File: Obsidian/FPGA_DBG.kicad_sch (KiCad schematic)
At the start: 24 parts, among them Q3 BSS138LT1G, SW1 SW_DIP_x01, U1 XC7A35T-CSG325, U27 S25FL128SAGMFI001, U9 REF3012

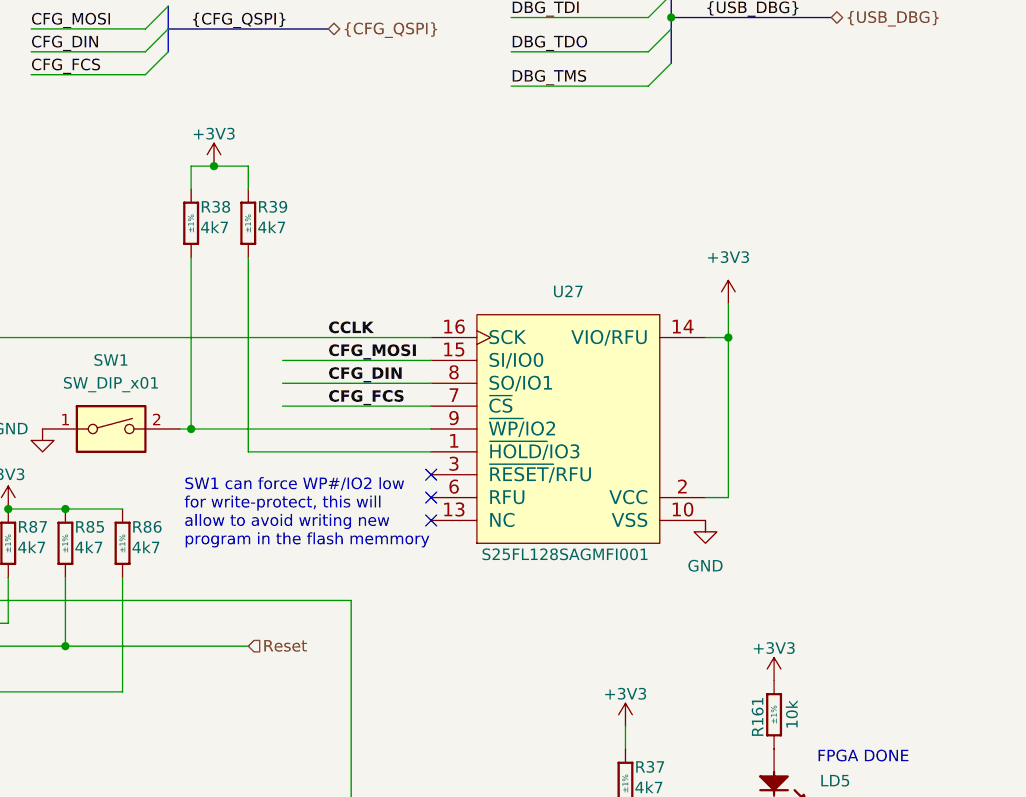
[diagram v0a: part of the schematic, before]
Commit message: Update TPSM863257RDXR symbol to set output pins as output power. Putting pull-up resistor on flash spi, decoupling capacitor and deconnect Vio.
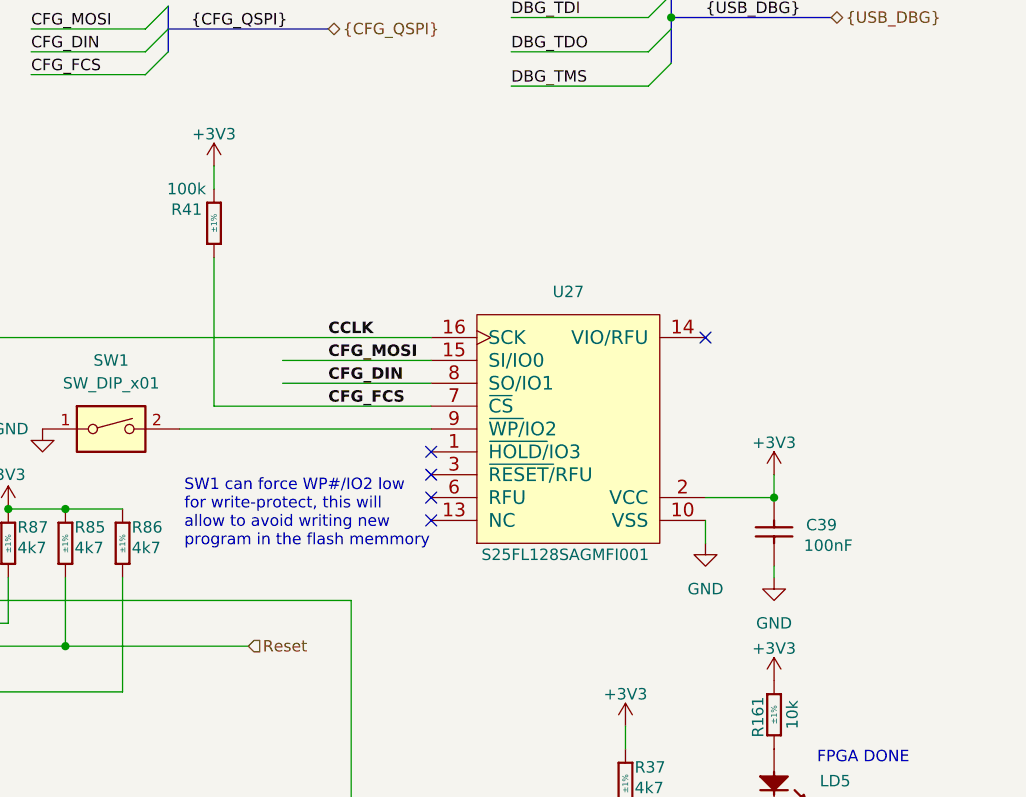
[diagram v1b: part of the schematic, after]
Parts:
- removed R38, R39: R0402_4K7_1%_0.0625W_100PPM, Footprint:RESC1005X40N, symbol Library_Symbol:R0402_4K7_1%_0.0625W_100PPM
- added C39: CC0201_100NF_6.3V_10%_X5R, Footprint:CAPC0603X33N, symbol Library_Symbol:CC0201_100NF_6.3V_10%_X5R
- added R41: R0402_100K_1%_0.0625W_100PPM, Footprint:RESC1005X40N, symbol Library_Symbol:R0402_100K_1%_0.0625W_100PPM
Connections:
- net +3V3: now also C39.1, R41.2; no longer U27.14 (VIO/RFU)
- net CFG_FCS: now also R41.1
- net GND: now also C39.2
- no-connect marks 3 -> 5

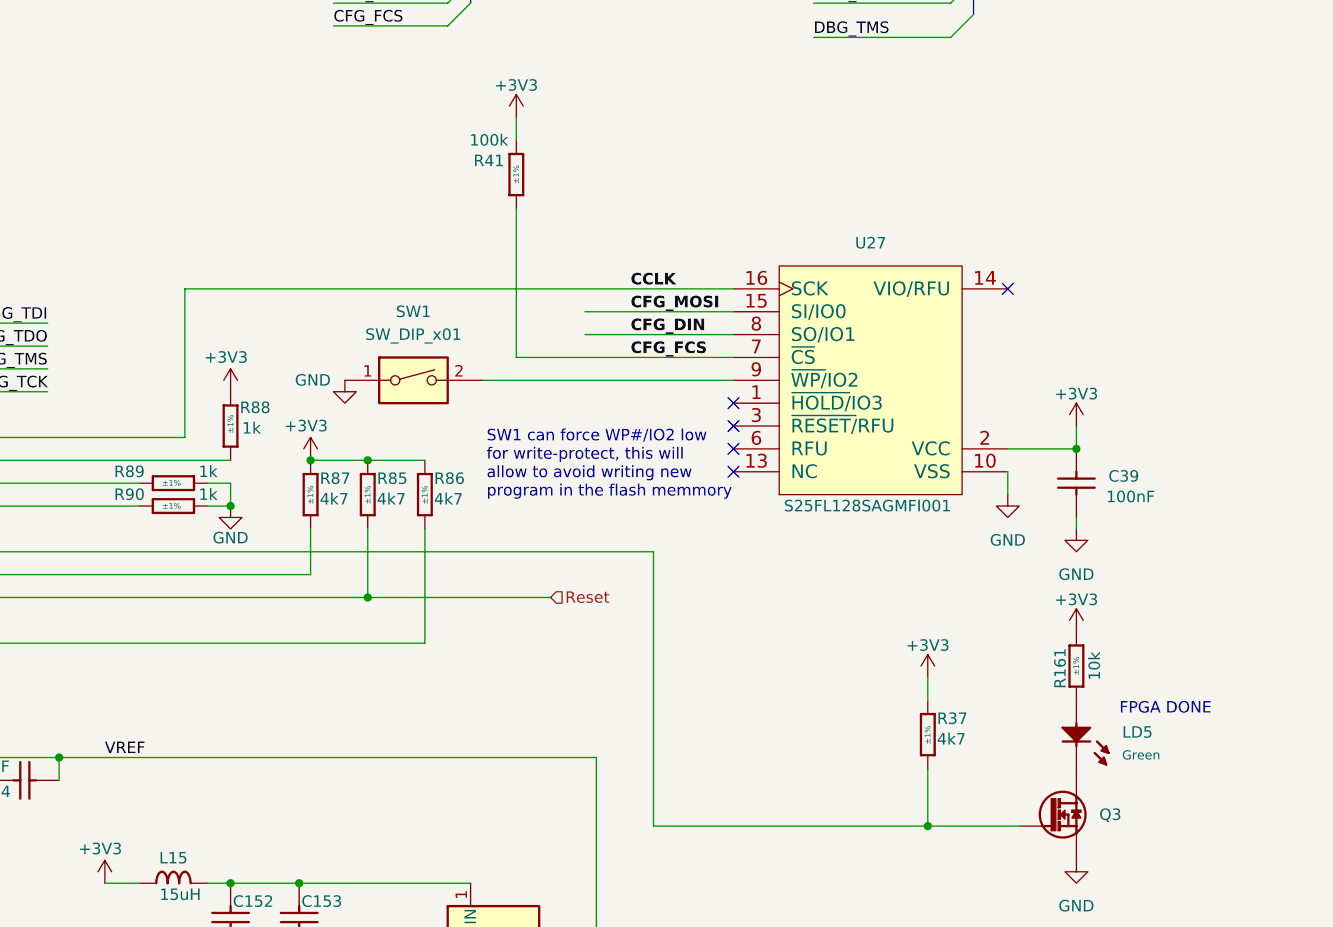
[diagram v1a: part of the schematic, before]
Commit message: Cleaning symbol fields
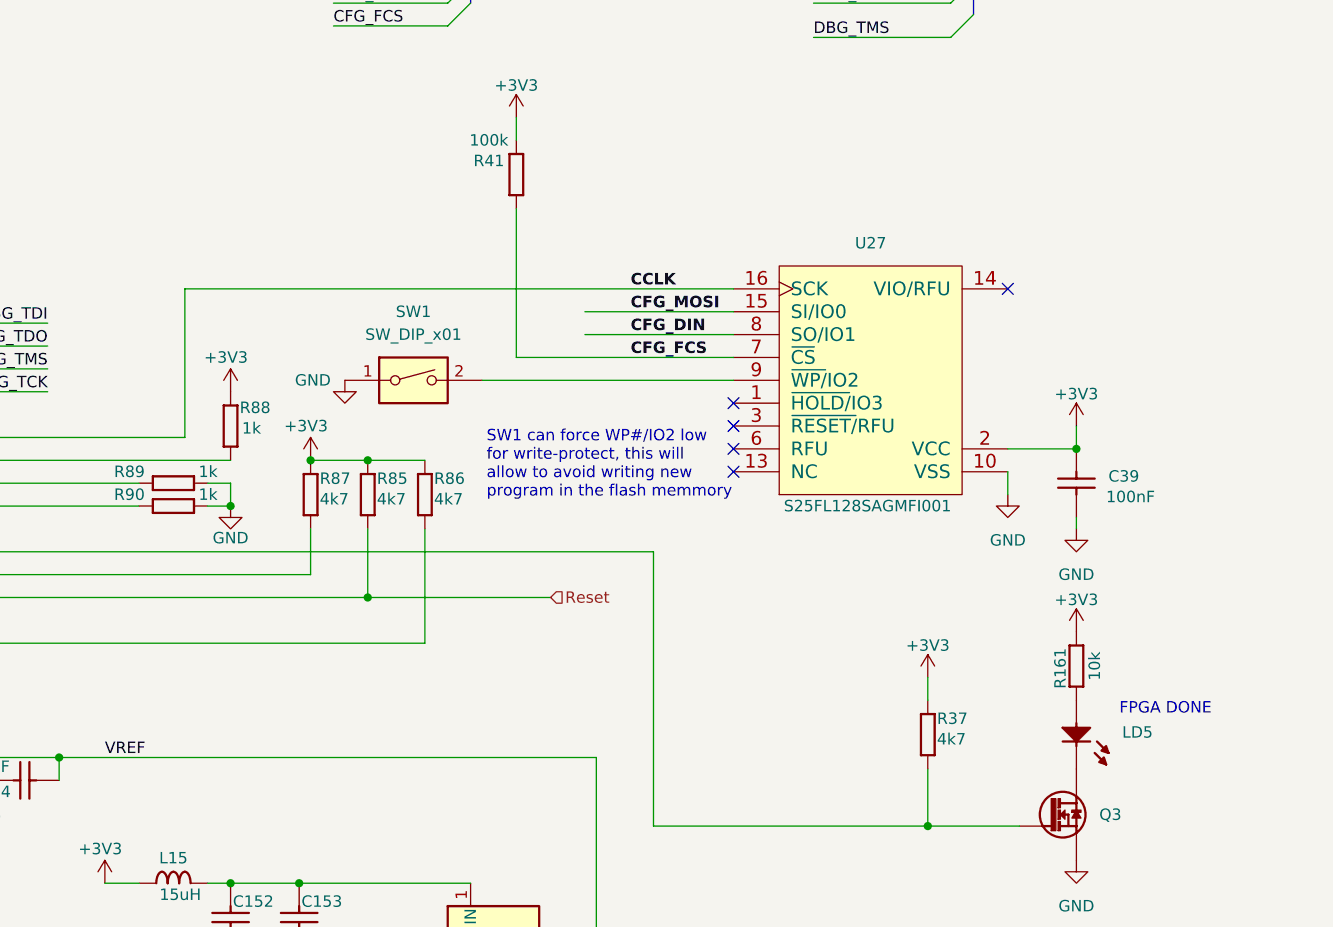
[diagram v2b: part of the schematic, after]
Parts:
- C146, C153: Author CERN DEM JLC -> (none); Case 0201 -> (none); Comment 470nF -> (none); Component Kind Standard -> (none); Component Type Standard -> (none); ComponentHeight (none) -> (none); CreateDate 05/27/10 00:00:00 -> (none); Database Table Name Capacitors -> (none); Footprint Library Capacitors SMD -> (none); Footprint Path PcbLib\Capacitors SMD.PcbLib -> (none); Footprint Ref CAPC0603X33N -> (none); HelpURL \\cern.ch\dfs\Applications\Altium\Datasheets\CC0201_X5R_TAI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 -> (none); LatestRevisionDate 05/27/10 00:00:00 -> (none); Library Name Capacitors SMD -> (none); Library Path SchLib\Capacitors.SchLib -> (none); Library Ref Capacitor - non polarized -> (none); License CC-BY-SA 4.0 -> (none); Manufacturer GENERIC -> (none); Manufacturer Part Number CC0201_470NF_4V_20%_X5R -> (none); Manufacturer1 ComponentHeight 0.33mm -> (none); Manufacturer1 Example TAIYO YUDEN -> (none); Manufacturer1 Part Number AMK063BJ474MP-F -> (none); Mounted Yes -> (none); PackageDescription (none) -> (none); Part Description SMD Multilayer Chip Ceramic Capacitor -> (none); Part Number CC0201_470NF_4V_20%_X5R -> (none); Pin Count 2 -> (none); PressFit (none) -> (none); SMD Yes -> (none); Sense No -> (none); Sense Comment (none) -> (none); Socket No -> (none); Status Not Recommended -> (none); Status Comment (none) -> (none); TC X5R -> (none); Tolerance ±20% -> (none); Voltage 4V -> (none)
- C150: Author CERN DEM JLC -> (none); Case 0201 -> (none); Comment 47nF -> (none); Component Kind Standard -> (none); Component Type Standard -> (none); ComponentHeight (none) -> (none); CreateDate 12/03/07 00:00:00 -> (none); Database Table Name Capacitors -> (none); Footprint Library Capacitors SMD -> (none); Footprint Path PcbLib\Capacitors SMD.PcbLib -> (none); Footprint Ref CAPC0603X33N -> (none); HelpURL \\cern.ch\dfs\Applications\Altium\Datasheets\CC0201_X5R_AVX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 -> (none); LatestRevisionDate 12/03/07 00:00:00 -> (none); Library Name Capacitors SMD -> (none); Library Path SchLib\Capacitors.SchLib -> (none); Library Ref Capacitor - non polarized -> (none); License CC-BY-SA 4.0 -> (none); Manufacturer GENERIC -> (none); Manufacturer Part Number CC0201_47NF_6.3V_10%_X5R -> (none); Manufacturer1 ComponentHeight 0.33mm -> (none); Manufacturer1 Example AVX -> (none); Manufacturer1 Part Number 02016D473KAT2A -> (none); Mounted Yes -> (none); PackageDescription (none) -> (none); Part Description SMD Multilayer Chip Ceramic Capacitor -> (none); Part Number CC0201_47NF_6.3V_10%_X5R -> (none); Pin Count 2 -> (none); PressFit (none) -> (none); SMD Yes -> (none); Sense No -> (none); Sense Comment (none) -> (none); Socket No -> (none); Status Not Recommended -> (none); Status Comment (none) -> (none); TC X5R -> (none); Tolerance ±10% -> (none); Voltage 6.3V -> (none)
- C151, C152: Author CERN DEM JLC -> (none); Case 0402 -> (none); Comment 10uF -> (none); Component Kind Standard -> (none); Component Type Standard -> (none); ComponentHeight (none) -> (none); CreateDate 01/07/15 00:00:00 -> (none); Database Table Name Capacitors -> (none); Footprint Library Capacitors SMD -> (none); Footprint Path PcbLib\Capacitors SMD.PcbLib -> (none); Footprint Ref CAPC1005X70N -> (none); HelpURL \\cern.ch\dfs\Applications\Altium\Datasheets\CC0402_X5R_TDK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 -> (none); LatestRevisionDate 01/07/15 00:00:00 -> (none); Library Name Capacitors SMD -> (none); Library Path SchLib\Capacitors.SchLib -> (none); Library Ref Capacitor - non polarized -> (none); License CC-BY-SA 4.0 -> (none); Manufacturer GENERIC -> (none); Manufacturer Part Number CC0402_10UF_6.3V_20%_X5R -> (none); Manufacturer1 ComponentHeight 0.70mm -> (none); Manufacturer1 Example TDK -> (none); Manufacturer1 Part Number C1005X5R0J106M050 -> (none); Mounted Yes -> (none); PackageDescription (none) -> (none); Part Description SMD Multilayer Chip Ceramic Capacitor -> (none); Part Number CC0402_10UF_6.3V_20%_X5R -> (none); Pin Count 2 -> (none); PressFit (none) -> (none); SMD Yes -> (none); Sense No -> (none); Sense Comment (none) -> (none); Socket No -> (none); Status Preferred -> (none); Status Comment (none) -> (none); TC X5R -> (none); Tolerance ±10% -> (none); Voltage 6.3V -> (none)
- C154, C39: Case 0201 -> (none); Comment =Value -> (none); Component Kind Standard -> (none); Component Type Standard -> (none); ComponentHeight (none) -> (none); CreateDate 12/03/07 00:00:00 -> (none); Footprint Path PcbLib\Capacitors SMD.PcbLib -> (none); Footprint Ref CAPC0603X33N -> (none); LatestRevisionDate 12/03/07 00:00:00 -> (none); Library Name Capacitors SMD -> (none); Library Path SchLib\Capacitors.SchLib -> (none); Library Ref Capacitor - non polarized -> (none); License This work is licensed under the Creative Commons CC-BY-SA 4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 -> (none); Manufacturer GENERIC -> (none); Manufacturer Part Number CC0201_100NF_6.3V_10%_X5R -> (none); Manufacturer1 ComponentHeight 0.33mm -> (none); Manufacturer1 Example AVX -> (none); Manufacturer1 Part Number 02016D104KAT2A -> (none); Mounted Yes -> (none); PackageDescription (none) -> (none); Part Description SMD Multilayer Chip Ceramic Capacitor -> (none); Part Number CC0201_100NF_6.3V_10%_X5R -> (none); Pin Count 2 -> (none); PressFit (none) -> (none); SMD Yes -> (none); Sense No -> (none); Sense Comment (none) -> (none); Socket No -> (none); Status Not Recommended -> (none); Status Comment (none) -> (none); TC X5R -> (none); Tolerance ±10% -> (none); Voltage 6.3V -> (none)
- L11: Author CERN DEM MR -> (none); Case 0603 -> (none); Comment 600R@100MHz -> (none); Component Kind Standard -> (none); Component Type Standard -> (none); ComponentHeight 0.95mm -> (none); CreateDate 04/01/16 00:00:00 -> (none); Database Table Name Inductors & Transformers -> (none); Footprint Library Inductors SMD -> (none); Footprint Path PcbLib\Inductors SMD.PcbLib -> (none); Footprint Ref INDC1608X95N -> (none); HelpURL \\cern.ch\dfs\Applications\Altium\Datasheets\IND0603_MURATA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 -> (none); LatestRevisionDate 10/25/18 00:00:00 -> (none); Library Name Inductors SMD -> (none); Library Path SchLib\Inductors & Transformers.SchLib -> (none); Library Ref Ferrite Bead -> (none); License CC-BY-SA 4.0 -> (none); Manufacturer MURATA -> (none); Manufacturer Part Number BLM18AG601SN1 -> (none); Mounted Yes -> (none); PackageDescription (none) -> (none); Part Description SMD EMIFIL Suppression Chip Ferrite Bead -> (none); Part Number IND0603_MURATA_BLM18AG601SN1 -> (none); Pin Count 2 -> (none); Power 500mA -> (none); Resistance 0.38R -> (none); SMD Yes -> (none); Sense No -> (none); Sense Comment (none) -> (none); Socket No -> (none); Status (none) -> (none); Status Comment (none) -> (none); Tolerance ±25% -> (none)
- L15: Author CERN DEM HF -> (none); Case 0805 -> (none); Comment 15uH -> (none); Component Kind Standard -> (none); Component Type Standard -> (none); ComponentHeight 1.45mm -> (none); CreateDate 04/18/24 00:00:00 -> (none); Database Table Name Inductors & Transformers -> (none); Footprint Library Inductors SMD -> (none); Footprint Path PcbLib\Inductors SMD.PcbLib -> (none); Footprint Ref INDC2013X145N -> (none); HelpURL \\cern.ch\dfs\Applications\Altium\Datasheets\IND0805_TDK_ML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 -> (none); LatestRevisionDate 04/18/24 00:00:00 -> (none); Library Name Inductors SMD -> (none); Library Path SchLib\Inductors & Transformers.SchLib -> (none); Library Ref Inductor -> (none); License CC-BY-SA 4.0 -> (none); Manufacturer TDK -> (none); Manufacturer Part Number MLZ2012M150WT000 -> (none); Mounted Yes -> (none); PackageDescription (none) -> (none); Part Description SMD Multilayer Ferrite (MLZ Series) -> (none); Part Number IND0805_TDK_MLZ2012M150WT000 -> (none); Pin Count 2 -> (none); Power 100mA -> (none); Resistance 0.95R -> (none); SMD Yes -> (none); Sense No -> (none); Sense Comment (none) -> (none); Socket No -> (none); Status (none) -> (none); Status Comment (none) -> (none); Tolerance ±20% -> (none)
- LD5: Author CERN DEM JLC -> (none); Bonding No -> (none); Case 0603 -> (none); Color Green -> (none); Comment (none) -> (none); Component Kind Standard -> (none); Component Type Standard -> (none); ComponentHeight 0.65mm -> (none); ComponentLink1Description (none) -> (none); ComponentLink1URL (none) -> (none); ComponentLink2Description (none) -> (none); ComponentLink2URL (none) -> (none); CreateDate 07/03/17 00:00:00 -> (none); Database Table Name ICs And Semiconductors -> (none); Device (none) -> (none); Footprint Library ICs And Semiconductors SMD -> (none); Footprint Path PcbLib\ICs And Semiconductors SMD.PcbLib -> (none); Footprint Ref LED_KINGBRIGHT_KPH-1608CGCK -> (none); HelpURL \\cern.ch\dfs\Applications\Altium\Datasheets\LED_KINGBRIGHT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 -> (none); LatestRevisionDate 07/03/17 00:00:00 -> (none); Library Name LEDs & Displays -> (none); Library Path SchLib\LEDs & Displays.SchLib -> (none); Library Ref LED Green 1C 2A -> (none); License CC-BY-SA 4.0 -> (none); Manufacturer KINGBRIGHT -> (none); Manufacturer Part Number KPH-1608CGCK -> (none); Mounted Yes -> (none); PackageDescription SMT Green LED, Case 0603, Body L 1.6 x W 0.8mm H 0.65mm -> (none); Part Description SMD Green LED, Case 1.6mmX0.8mm(0603), 0.65mm Thickness -> (none); Part Number LED_KINGBRIGHT_KPH-1608CGCK -> (none); Pin Count 2 -> (none); PressFit No -> (none); SMD Yes -> (none); Sense No -> (none); Sense Comment (none) -> (none); Socket No -> (none); Status (none) -> (none); Status Comment (none) -> (none)
- Q3: Author CERN DEM JLC -> (none); Bonding No -> (none); Case SOT23-3 -> (none); Comment BSS138LT1G -> (none); Component Kind Standard -> (none); Component Type Standard -> (none); ComponentHeight 1.11mm -> (none); ComponentLink1Description (none) -> (none); ComponentLink1URL (none) -> (none); ComponentLink2Description (none) -> (none); ComponentLink2URL (none) -> (none); CreateDate 03/23/09 00:00:00 -> (none); Database Table Name ICs And Semiconductors -> (none); Device BSS138LT1G -> (none); Footprint Library ICs And Semiconductors SMD -> (none); Footprint Path PcbLib\ICs And Semiconductors SMD.PcbLib -> (none); Footprint Ref SOT95P240X110-3N -> (none); HelpURL \\cern.ch\dfs\Applications\Altium\Datasheets\BSS138LT1G.pdf -> (none); LatestRevisionDate 05/25/22 00:00:00 -> (none); LatestRevisionDate1 (none) -> (none); Library Name Transistors -> (none); Library Path SchLib\Transistors.SchLib -> (none); Library Ref N-MOSFET-D 1G 2S 3D -> (none); License CC-BY-SA 4.0 -> (none); Manufacturer ON SEMICONDUCTOR -> (none); Manufacturer Part Number BSS138L -> (none); Mounted Yes -> (none); PackageDescription SOT23, 0.95mm Pitch; 3 Pin, 1.40mm W X 3.00mm L X 1.10mm H 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 -> (none); Part Description 50V, 200mA N-Channel Enhancement Mode Field-Effect Transist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 -> (none); Part Number BSS138LT1G -> (none); Pin Count 3 -> (none); PressFit No -> (none); SCEM (none) -> (none); SMD Yes -> (none); Sense No -> (none); Sense Comment (none) -> (none); Socket No -> (none); Status (none) -> (none); Status Comment (none) -> (none)
- R161: Author CERN DEM JLC -> (none); Case 0402 -> (none); Comment 10k -> (none); Component Kind Standard -> (none); Component Type Standard -> (none); ComponentHeight (none) -> (none); CreateDate 12/03/07 00:00:00 -> (none); Database Table Name Resistors -> (none); Footprint Library Resistors SMD -> (none); Footprint Path PcbLib\Resistors SMD.PcbLib -> (none); Footprint Ref RESC1005X40N -> (none); HelpURL \\cern.ch\dfs\Applications\Altium\Datasheets\R0402_Phycomp_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 -> (none); LatestRevisionDate 10/17/12 00:00:00 -> (none); Library Name Resistors SMD -> (none); Library Path SchLib\Resistors.SchLib -> (none); Library Ref Resistor - 1% -> (none); License CC-BY-SA 4.0 -> (none); Manufacturer GENERIC -> (none); Manufacturer Part Number R0402_10K_1%_0.0625W_100PPM -> (none); Manufacturer1 ComponentHeight 0.4mm -> (none); Manufacturer1 Example YAGEO PHYCOMP -> (none); Manufacturer1 Part Number 232270671003L -> (none); Mounted Yes -> (none); PackageDescription (none) -> (none); Part Description General Purpose Thick Film Chip Resistor -> (none); Part Number R0402_10K_1%_0.0625W_100PPM -> (none); Pin Count 2 -> (none); Power 0.0625W -> (none); PressFit No -> (none); SMD Yes -> (none); Sense No -> (none); Sense Comment (none) -> (none); Socket No -> (none); Status Not Recommended -> (none); Status Comment (none) -> (none); TC ±100ppm/°C -> (none); Tolerance ±1% -> (none); Voltage (none) -> (none)
- R37, R85, R86, R87: Author CERN DEM JLC -> (none); Case 0402 -> (none); Comment 4k7 -> (none); Component Kind Standard -> (none); Component Type Standard -> (none); ComponentHeight (none) -> (none); CreateDate 12/03/07 00:00:00 -> (none); Database Table Name Resistors -> (none); Footprint Library Resistors SMD -> (none); Footprint Path PcbLib\Resistors SMD.PcbLib -> (none); Footprint Ref RESC1005X40N -> (none); HelpURL \\cern.ch\dfs\Applications\Altium\Datasheets\R0402_Phycomp_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 -> (none); LatestRevisionDate 10/17/12 00:00:00 -> (none); Library Name Resistors SMD -> (none); Library Path SchLib\Resistors.SchLib -> (none); Library Ref Resistor - 1% -> (none); License CC-BY-SA 4.0 -> (none); Manufacturer GENERIC -> (none); Manufacturer Part Number R0402_4K7_1%_0.0625W_100PPM -> (none); Manufacturer1 ComponentHeight 0.4mm -> (none); Manufacturer1 Example YAGEO PHYCOMP -> (none); Manufacturer1 Part Number 232270674702L -> (none); Mounted Yes -> (none); PackageDescription (none) -> (none); Part Description General Purpose Thick Film Chip Resistor -> (none); Part Number R0402_4K7_1%_0.0625W_100PPM -> (none); Pin Count 2 -> (none); Power 0.0625W -> (none); PressFit No -> (none); SMD Yes -> (none); Sense No -> (none); Sense Comment (none) -> (none); Socket No -> (none); Status Not Recommended -> (none); Status Comment (none) -> (none); TC ±100ppm/°C -> (none); Tolerance ±1% -> (none); Voltage (none) -> (none)
- R41: Author CERN DEM JLC -> (none); Case 0402 -> (none); Comment 100k -> (none); Component Kind Standard -> (none); Component Type Standard -> (none); ComponentHeight (none) -> (none); CreateDate 12/03/07 00:00:00 -> (none); Database Table Name Resistors -> (none); Footprint Library Resistors SMD -> (none); Footprint Path PcbLib\Resistors SMD.PcbLib -> (none); Footprint Ref RESC1005X40N -> (none); HelpURL \\cern.ch\dfs\Applications\Altium\Datasheets\R0402_Phycomp_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 -> (none); LatestRevisionDate 10/17/12 00:00:00 -> (none); Library Name Resistors SMD -> (none); Library Path SchLib\Resistors.SchLib -> (none); Library Ref Resistor - 1% -> (none); License CC-BY-SA 4.0 -> (none); Manufacturer GENERIC -> (none); Manufacturer Part Number R0402_100K_1%_0.0625W_100PPM -> (none); Manufacturer1 ComponentHeight 0.4mm -> (none); Manufacturer1 Example YAGEO PHYCOMP -> (none); Manufacturer1 Part Number 232270671004L -> (none); Mounted Yes -> (none); PackageDescription (none) -> (none); Part Description General Purpose Thick Film Chip Resistor -> (none); Part Number R0402_100K_1%_0.0625W_100PPM -> (none); Pin Count 2 -> (none); Power 0.0625W -> (none); PressFit No -> (none); SMD Yes -> (none); Sense No -> (none); Sense Comment (none) -> (none); Socket No -> (none); Status Not Recommended -> (none); Status Comment (none) -> (none); TC ±100ppm/°C -> (none); Tolerance ±1% -> (none); Voltage (none) -> (none)
- R88, R89, R90: Author CERN DEM JLC -> (none); Case 0402 -> (none); Comment 1k -> (none); Component Kind Standard -> (none); Component Type Standard -> (none); ComponentHeight (none) -> (none); CreateDate 12/03/07 00:00:00 -> (none); Database Table Name Resistors -> (none); Footprint Library Resistors SMD -> (none); Footprint Path PcbLib\Resistors SMD.PcbLib -> (none); Footprint Ref RESC1005X40N -> (none); HelpURL \\cern.ch\dfs\Applications\Altium\Datasheets\R0402_Phycomp_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 -> (none); LatestRevisionDate 10/17/12 00:00:00 -> (none); Library Name Resistors SMD -> (none); Library Path SchLib\Resistors.SchLib -> (none); Library Ref Resistor - 1% -> (none); License CC-BY-SA 4.0 -> (none); Manufacturer GENERIC -> (none); Manufacturer Part Number R0402_1K_1%_0.0625W_100PPM -> (none); Manufacturer1 ComponentHeight 0.4mm -> (none); Manufacturer1 Example YAGEO PHYCOMP -> (none); Manufacturer1 Part Number 232270671002L -> (none); Mounted Yes -> (none); PackageDescription (none) -> (none); Part Description General Purpose Thick Film Chip Resistor -> (none); Part Number R0402_1K_1%_0.0625W_100PPM -> (none); Pin Count 2 -> (none); Power 0.0625W -> (none); PressFit No -> (none); SMD Yes -> (none); Sense No -> (none); Sense Comment (none) -> (none); Socket No -> (none); Status Not Recommended -> (none); Status Comment (none) -> (none); TC ±100ppm/°C -> (none); Tolerance ±1% -> (none); Voltage (none) -> (none)
- U27: Author CERN DEM JLC -> (none); Bonding No -> (none); Case SOIC16 -> (none); Comment S25FL128SAGMFI001 -> (none); Component Kind Standard -> (none); Component Type Standard -> (none); ComponentHeight 2.65mm -> (none); ComponentLink1Description (none) -> (none); ComponentLink1URL (none) -> (none); ComponentLink2Description (none) -> (none); ComponentLink2URL (none) -> (none); CreateDate 07/11/18 00:00:00 -> (none); Database Table Name ICs And Semiconductors -> (none); Device S25FL128SAGMFI001 -> (none); Footprint Library ICs And Semiconductors SMD -> (none); Footprint Path PcbLib\ICs And Semiconductors SMD.PcbLib -> (none); Footprint Ref SOIC127P1030X265-16N -> (none); HelpURL \\cern.ch\dfs\Applications\Altium\Datasheets\S25FL128SAGMFI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 -> (none); LatestRevisionDate 07/11/18 00:00:00 -> (none); Library Name Logic -> (none); Library Path SchLib\Logic.SchLib -> (none); Library Ref S25FL128SAGMFI001 -> (none); License CC-BY-SA 4.0 -> (none); Manufacturer CYPRESS -> (none); Manufacturer Part Number S25FL128SAGMFI001 -> (none); Mounted Yes -> (none); PackageDescription SOIC, 1.27mm Pitch; 16 Pin, 7.50mm W X 10.3mm L X 2.65mm H 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 -> (none); Part Description 128Mbit, 133MHz, MirrorBit® Flash Non-Volatile Memory CMOS 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 -> (none); Part Number S25FL128SAGMFI001 -> (none); Pin Count 11 -> (none); PressFit No -> (none); SCEM (none) -> (none); SMD Yes -> (none); Sense No -> (none); Sense Comment (none) -> (none); Socket No -> (none); Status (none) -> (none); Status Comment (none) -> (none)
